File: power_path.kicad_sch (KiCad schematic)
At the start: 0 parts

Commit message: Added TPS631000
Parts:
- added U2: TPS631000DRLR, footprints:SOT50P160X60-8N, symbol symbols:TPS631000DRLR
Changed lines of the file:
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@@
 	(generator_version "10.0")
 	(paper "A4")
+	(symbol
+		(lib_id "symbols:TPS631000DRLR")
+		(at 85.09 72.39 0)
+		(unit 1)
+		(body_style 1)
+		(exclude_from_sim no)
+		(in_bom yes)
+		(on_board yes)
+		(in_pos_files yes)
+		(dnp no)
+		(fields_autoplaced yes)
+		(property "Reference" "U2"
+			(at 85.09 54.61 0)
+			(show_name no)
+			(do_not_autoplace no)
+			(effects
+				(font
+					(size 1.27 1.27)
+				)
+			)
+		)
+		(property "Value" "TPS631000DRLR"
+			(at 85.09 57.15 0)
+			(show_name no)
+			(do_not_autoplace no)
+			(effects
+				(font
+					(size 1.27 1.27)
+				)
+			)
+		)
+		(property "Footprint" "footprints:SOT50P160X60-8N"
+			(at 85.09 72.39 0)
+			(hide yes)
+			(show_name no)
+			(do_not_autoplace no)
+			(effects
+				(font
+					(size 1.27 1.27)
+				)
+				(justify bottom)
+			)
+		)
+		(property "Datasheet" ""
+			(at 85.09 72.39 0)
+			(hide yes)
+			(show_name no)
+			(do_not_autoplace no)
+			(effects
+				(font
+					(size 1.27 1.27)
+				)
+			)
+		)
+		(property "Description" "1.5-A output current, high-power-density buck-boost converter"
+			(at 85.09 72.39 0)
+			(hide yes)
+			(show_name no)
+			(do_not_autoplace no)
+			(effects
+				(font
+					(size 1.27 1.27)
+				)
+				(justify bottom)
+			)
+		)
+		(property "DigiKey_Part_Number" "296-TPS631000DRLRCT-ND"
+			(at 85.09 72.39 0)
+			(hide yes)
+			(show_name no)
+			(do_not_autoplace no)
+			(effects
+				(font
+					(size 1.27 1.27)
+				)
+				(justify bottom)
+			)
+		)
+		(property "SnapEDA_Link" "https://www.snapeda.com/parts/TPS631000DRLR/Texas+Instruments/view-part/?ref=snap"
+			(at 85.09 72.39 0)
+			(hide yes)
+			(show_name no)
+			(do_not_autoplace no)
+			(effects
+				(font
+					(size 1.27 1.27)
+				)
+				(justify bottom)
+			)
+		)
+		(property "SNAPEDA_PACKAGE_ID" "124400"
+			(at 85.09 72.39 0)
+			(hide yes)
+			(show_name no)
+			(do_not_autoplace no)
+			(effects
+				(font
+					(size 1.27 1.27)
+				)
+				(justify bottom)
+			)
+		)
+		(property "Package" "SOT-583 Texas Instruments"
+			(at 85.09 72.39 0)
+			(hide yes)
+			(show_name no)
+			(do_not_autoplace no)
+			(effects
+				(font
+					(size 1.27 1.27)
+				)
+				(justify bottom)
+			)
+		)
+		(property "Check_prices" "https://www.snapeda.com/parts/TPS631000DRLR/Texas+Instruments/view-part/?ref=eda"
+			(at 85.09 72.39 0)
+			(hide yes)
+			(show_name no)
+			(do_not_autoplace no)
+			(effects
+				(font
+					(size 1.27 1.27)
+				)
+				(justify bottom)
+			)
+		)
+		(property "STANDARD" "IPC 7351B"
+			(at 85.09 72.39 0)
+			(hide yes)
+			(show_name no)
+			(do_not_autoplace no)
+			(effects
+				(font
+					(size 1.27 1.27)
+				)
+				(justify bottom)
+			)
+		)
+		(property "PARTREV" "B"
+			(at 85.09 72.39 0)
+			(hide yes)
+			(show_name no)
+			(do_not_autoplace no)
+			(effects
+				(font
+					(size 1.27 1.27)
+				)
+				(justify bottom)
+			)
+		)
+		(property "MF" "Texas Instruments"
+			(at 85.09 72.39 0)
+			(hide yes)
+			(show_name no)
+			(do_not_autoplace no)
+			(effects
+				(font
+					(size 1.27 1.27)
+				)
+				(justify bottom)
+			)
+		)
+		(property "MP" "TPS631000DRLR"
+			(at 85.09 72.39 0)
+			(hide yes)
+			(show_name no)
+			(do_not_autoplace no)
+			(effects
+				(font
+					(size 1.27 1.27)
+				)
+				(justify bottom)
+			)
+		)
+		(property "MANUFACTURER" "Texas Instruments"
+			(at 85.09 72.39 0)
+			(hide yes)
+			(show_name no)
+			(do_not_autoplace no)
+			(effects
+				(font
+					(size 1.27 1.27)
+				)
+				(justify bottom)
+			)
+		)
+		(property "MAXIMUM_PACKAGE_HEIGHT" "0.6mm"
+			(at 85.09 72.39 0)
+			(hide yes)
+			(show_name no)
+			(do_not_autoplace no)
+			(effects
+				(font
+					(size 1.27 1.27)
+				)
+				(justify bottom)
+			)
+		)
+		(property "LCSC" "C5219190"
+			(at 85.09 72.39 0)
+			(hide yes)
+			(show_name no)
+			(do_not_autoplace no)
+			(effects
+				(font
+					(size 1.27 1.27)
+				)
+			)
+		)
+		(pin "7"
+		)
+		(pin "8"
+		)
+		(pin "6"
+		)
+		(pin "4"
+		)
+		(pin "3"
+		)
+		(pin "2"
+		)
+		(pin "5"
+		)
+		(pin "1"
+		)
+		(instances
+			(project "pedal"
+				(path "/e2443317-b83f-4e66-ac79-3186c6d613f3/487ab5a8-1c1d-4a3e-8f62-a21afc38e9a3"
+					(reference "U2")
+					(unit 1)
+				)
+			)
+		)
+	)
 )

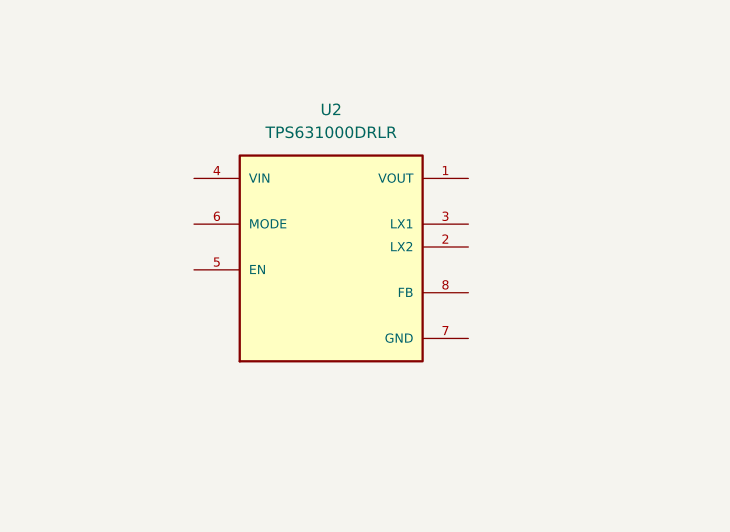
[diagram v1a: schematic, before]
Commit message: buck boost regulator schematic done
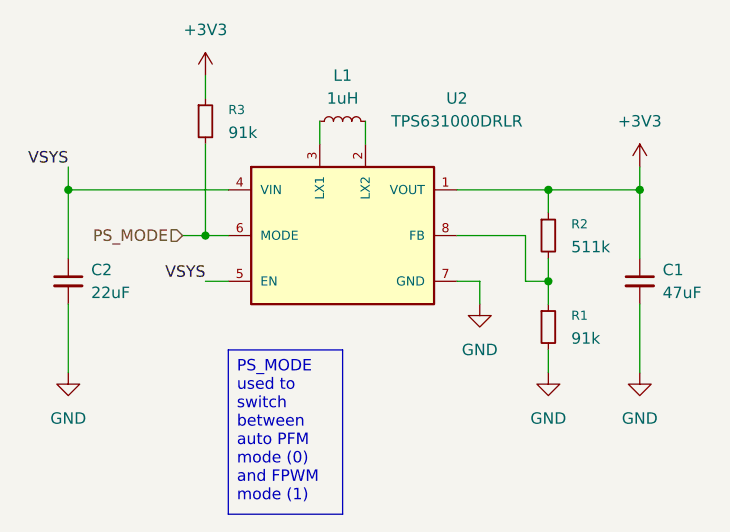
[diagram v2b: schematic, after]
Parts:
- added C1: 47uF, Capacitor_SMD:C_0805_2012Metric, symbol Device:C_Small
- added C2: 22uF, Capacitor_SMD:C_1206_3216Metric, symbol Device:C_Small
- added L1: 1uH, Inductor_SMD:L_1008_2520Metric, symbol Device:L_Small
- added R1, R3: 91k, Resistor_SMD:R_0402_1005Metric, symbol Device:R_Small
- added R2: 511k, Resistor_SMD:R_0402_1005Metric, symbol Device:R_Small
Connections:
- net +3V3: now reaches U2.1 (VOUT)
- net +3V3: now also C1.1, R2.1, R3.1
- net at U2.2 (LX2): now also L1.2
- net at U2.3 (LX1): now also L1.1
- net VSYS: now reaches U2.4 (VIN)
- net VSYS: now also U2.5 (EN), C2.1
- net PS_MODE: now reaches U2.6 (MODE)
- net PS_MODE: now also R3.2
- net GND: now reaches U2.7 (GND)
- net GND: now also C1.2, C2.2, R1.2
- net at U2.8 (FB): now also R1.1, R2.2
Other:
- moved on the sheet: U2

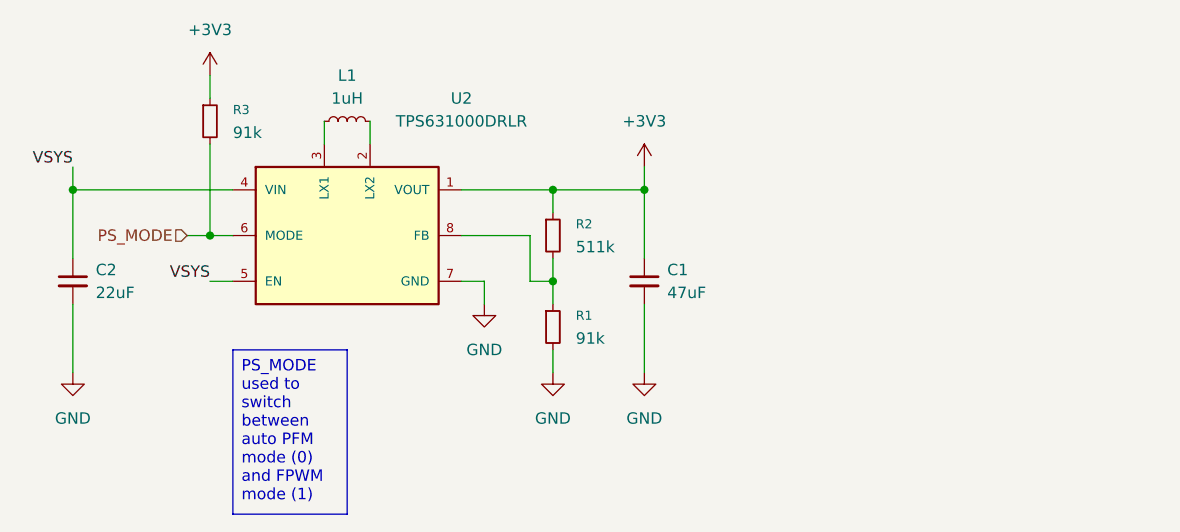
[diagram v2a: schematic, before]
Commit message: added LDO for LCD rail
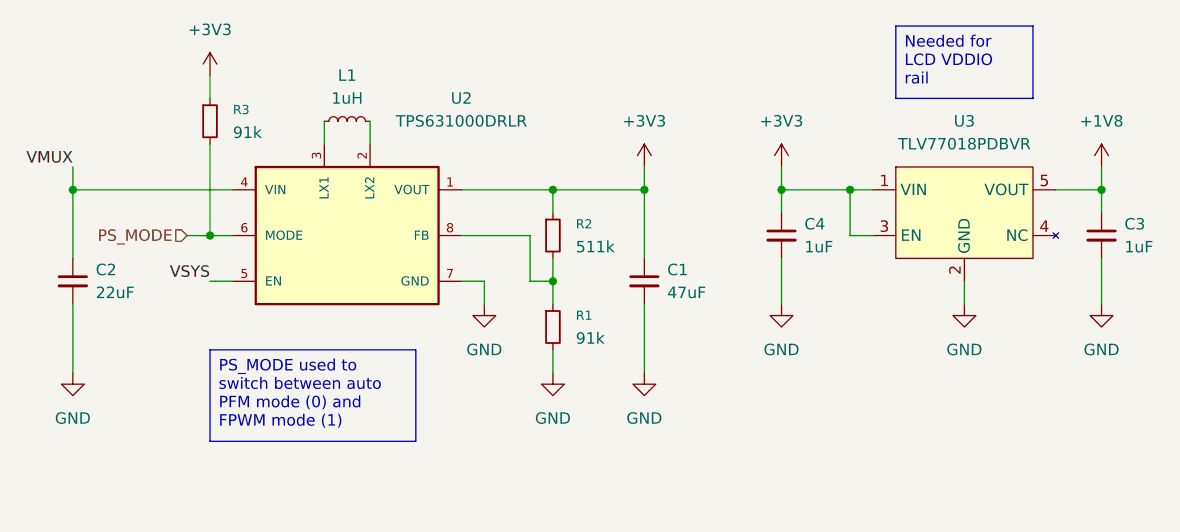
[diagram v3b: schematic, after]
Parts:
- added C3, C4: 1uF, Capacitor_SMD:C_0402_1005Metric, symbol Device:C_Small
- added U3: TLV77018PDBVR, Package_TO_SOT_SMD:SOT-23-5, symbol symbols:TLV77018PDBVR
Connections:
- net +3V3: now also C4.1, U3.1 (VIN), U3.3 (EN)
- net GND: now also C3.2, C4.2, U3.2 (GND)
- net VSYS: no longer C2.1, U2.4 (VIN)
- new net +1V8: C3.1, U3.5 (VOUT)
- new net VMUX: C2.1, U2.4 (VIN)

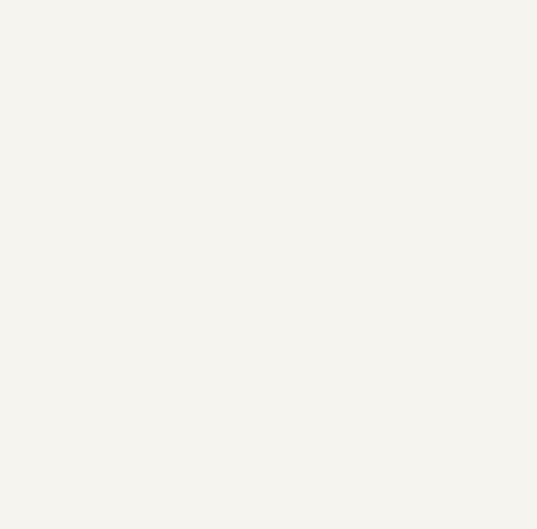
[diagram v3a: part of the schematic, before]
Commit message: add tps2121 power mux component
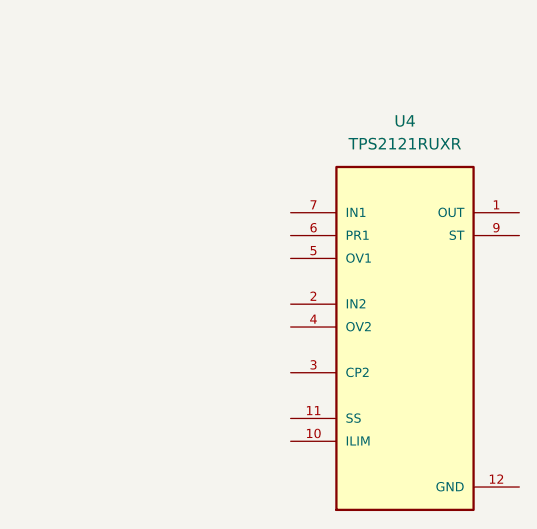
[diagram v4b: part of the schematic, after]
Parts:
- added U4: TPS2121RUXR, footprints:IC_TPS2121RUXR, symbol symbols:TPS2121RUXR
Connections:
- new net: U4.1 (OUT), U4.1_1 (OUT), U4.8 (OUT), U4.8_1 (OUT)
- new net: U4.2 (IN2), U4.2_1 (IN2)
- new net: U4.7 (IN1), U4.7_1 (IN1)
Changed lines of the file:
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@@
+	)
+	(symbol
+		(lib_id "symbols:TPS2121RUXR")
+		(at 223.52 81.28 0)
+		(unit 1)
+		(body_style 1)
+		(exclude_from_sim no)
+		(in_bom yes)
+		(on_board yes)
+		(in_pos_files yes)
+		(dnp no)
+		(fields_autoplaced yes)
+		(property "Reference" "U4"
+			(at 223.52 55.88 0)
+			(show_name no)
+			(do_not_autoplace no)
+			(effects
+				(font
+					(size 1.27 1.27)
+				)
+			)
+		)
+		(property "Value" "TPS2121RUXR"
+			(at 223.52 58.42 0)
+			(show_name no)
+			(do_not_autoplace no)
+			(effects
+				(font
+					(size 1.27 1.27)
+				)
+			)
+		)
+		(property "Footprint" "footprints:IC_TPS2121RUXR"
+			(at 223.52 81.28 0)
+			(hide yes)
+			(show_name no)
+			(do_not_autoplace no)
+			(effects
+				(font
+					(size 1.27 1.27)
+				)
+				(justify bottom)
+			)
+		)
+		(property "Datasheet" ""
+			(at 223.52 81.28 0)
+			(hide yes)
+			(show_name no)
+			(do_not_autoplace no)
+			(effects
+				(font
+					(size 1.27 1.27)
+				)
+			)
+		)
+		(property "Description" "2.7-V to 22-V, 56-mΩ, 4.5-A, power mux with seamless switchover"
+			(at 223.52 81.28 0)
+			(hide yes)
+			(show_name no)
+			(do_not_autoplace no)
+			(effects
+				(font
+					(size 1.27 1.27)
+				)
+				(justify bottom)
+			)
+		)
+		(property "MF" "Texas Instruments"
+			(at 223.52 81.28 0)
+			(hide yes)
+			(show_name no)
+			(do_not_autoplace no)
+			(effects
+				(font
+					(size 1.27 1.27)
+				)
+				(justify bottom)
+			)
+		)
+		(property "Package" "VQFN-HR-12 Texas Instruments"
+			(at 223.52 81.28 0)
+			(hide yes)
+			(show_name no)
+			(do_not_autoplace no)
+			(effects
+				(font
+					(size 1.27 1.27)
+				)
+				(justify bottom)
+			)
+		)
+		(property "Price" "None"
+			(at 223.52 81.28 0)
+			(hide yes)
+			(show_name no)
+			(do_not_autoplace no)
+			(effects
+				(font
+					(size 1.27 1.27)
+				)
+				(justify bottom)
+			)
+		)
+		(property "Check_prices" "https://www.snapeda.com/parts/TPS2121RUXR/Texas+Instruments/view-part/?ref=eda"
+			(at 223.52 81.28 0)
+			(hide yes)
+			(show_name no)
+			(do_not_autoplace no)
+			(effects
+				(font
+					(size 1.27 1.27)
+				)
+				(justify bottom)
+			)
+		)
+		(property "STANDARD" "Manufacturer Recommendations"
+			(at 223.52 81.28 0)
+			(hide yes)
+			(show_name no)
+			(do_not_autoplace no)
+			(effects
+				(font
+					(size 1.27 1.27)
+				)
+				(justify bottom)
+			)
+		)
+		(property "SnapEDA_Link" "https://www.snapeda.com/parts/TPS2121RUXR/Texas+Instruments/view-part/?ref=snap"
+			(at 223.52 81.28 0)
+			(hide yes)
+			(show_name no)
+			(do_not_autoplace no)
+			(effects
+				(font
+					(size 1.27 1.27)
+				)
+				(justify bottom)
+			)
+		)
+		(property "MP" "TPS2121RUXR"
+			(at 223.52 81.28 0)
+			(hide yes)
+			(show_name no)
+			(do_not_autoplace no)
+			(effects
+				(font
+					(size 1.27 1.27)
+				)
+				(justify bottom)
+			)
+		)
+		(property "Availability" "In Stock"
+			(at 223.52 81.28 0)
+			(hide yes)
+			(show_name no)
+			(do_not_autoplace no)
+			(effects
+				(font
+					(size 1.27 1.27)
+				)
+				(justify bottom)
+			)
+		)
+		(property "MANUFACTURER" "TEXAS INSTRUMENTS"
+			(at 223.52 81.28 0)
+			(hide yes)
+			(show_name no)
+			(do_not_autoplace no)
+			(effects
+				(font
+					(size 1.27 1.27)
+				)
+				(justify bottom)
+			)
+		)
+		(property "LCSC" "C485916"
+			(at 223.52 81.28 0)
+			(hide yes)
+			(show_name no)
+			(do_not_autoplace no)
+			(effects
+				(font
+					(size 1.27 1.27)
+				)
+			)
+		)
+		(pin "8"
+		)
+		(pin "11"
+		)
+		(pin "7_1"
+		)
+		(pin "9"
+		)
+		(pin "10"
+		)
+		(pin "12"
+		)
+		(pin "8_1"
+		)
+		(pin "2"
+		)
+		(pin "5"
+		)
+		(pin "2_1"
+		)
+		(pin "3"
+		)
+		(pin "4"
+		)
+		(pin "7"
+		)
+		(pin "6"
+		)
+		(pin "1"
+		)
+		(pin "1_1"
+		)
+		(instances
+			(project "pedal"
+				(path "/e2443317-b83f-4e66-ac79-3186c6d613f3/487ab5a8-1c1d-4a3e-8f62-a21afc38e9a3"
+					(reference "U4")
+					(unit 1)
+				)
+			)
+		)
 	)
 	(symbol

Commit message: wip
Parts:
- added R4: 56k, Resistor_SMD:R_0402_1005Metric, symbol Device:R_Small
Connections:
- net GND: now also U4.3 (CP2), U4.6 (PR1), R4.2
- net VMUX: now also U4.1 (OUT), U4.1_1 (OUT), U4.8 (OUT), U4.8_1 (OUT)
- net at U4.10 (ILIM): now also R4.1
- net VUSB: now reaches U4.7 (IN1), U4.7_1 (IN1)

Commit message: random silly commit
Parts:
- removed R4: 56k, Resistor_SMD:R_0402_1005Metric, symbol Device:R_Small
- removed U4: TPS2121RUXR, footprints:IC_TPS2121RUXR, symbol symbols:TPS2121RUXR
- added U4: TPS2116DRL, Package_TO_SOT_SMD:SOT-583-8, symbol Power_Management:TPS2116DRL
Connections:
- net VSYS is gone; now on net VMUX: U2.5 (EN)
- net GND: now also U4.1 (GND)
- net VMUX: now also U4.2 (VOUT), U4.7 (VOUT)
- net VUSB: now also U4.3 (VIN1), U4.4 (PR1), U4.5 (MODE)
- new net MUX_STATE: U4.8 (ST)
- new net VBATT: U4.6 (VIN2)
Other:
- note added: "Low: Battery, Hi-Z: USB"
- note added: "Low: PFM, Hi-Z: FPWM"

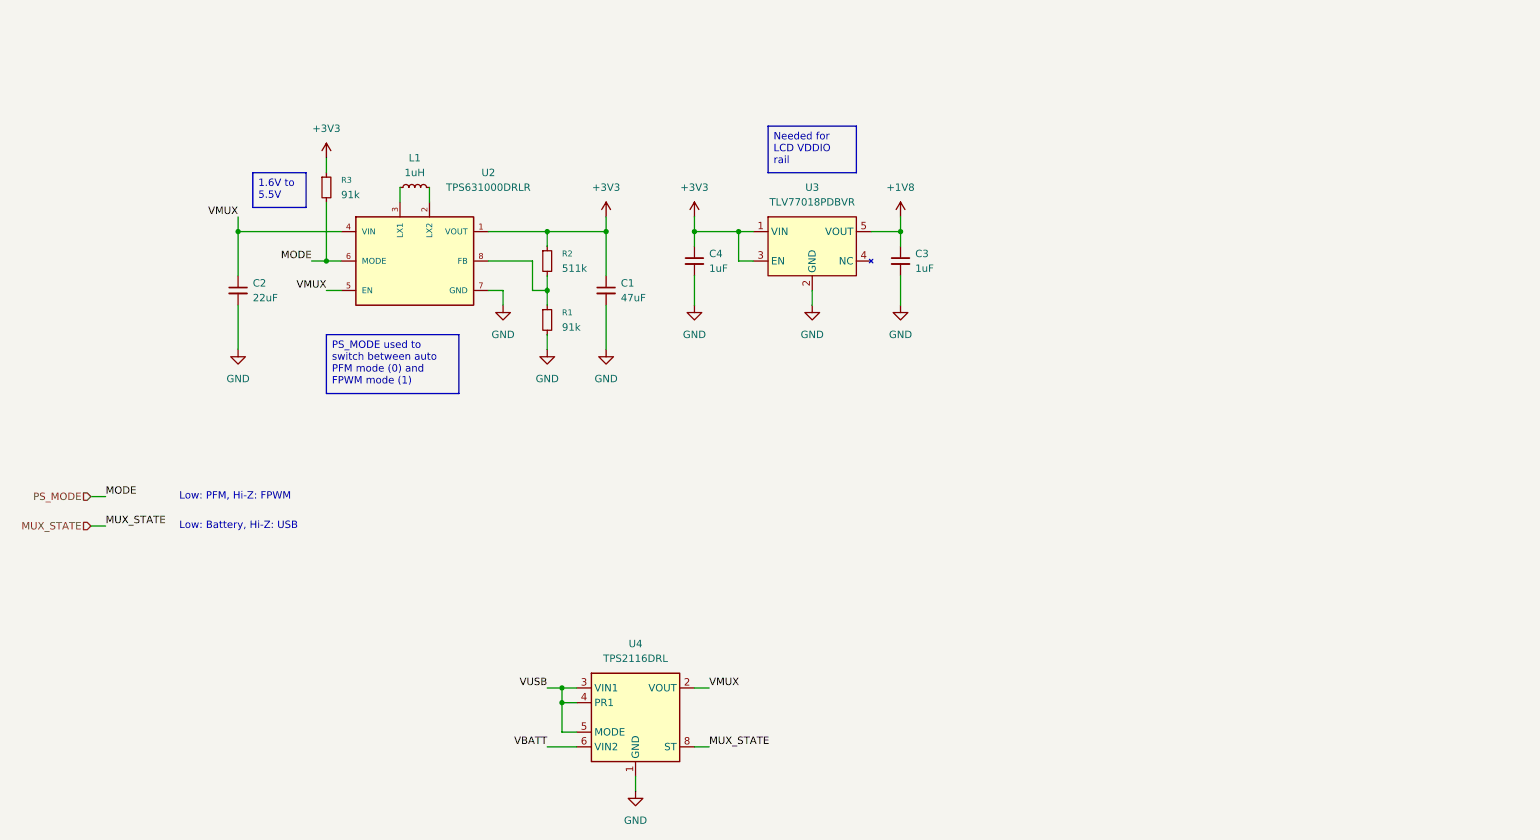
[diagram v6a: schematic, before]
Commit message: add type c receptacle
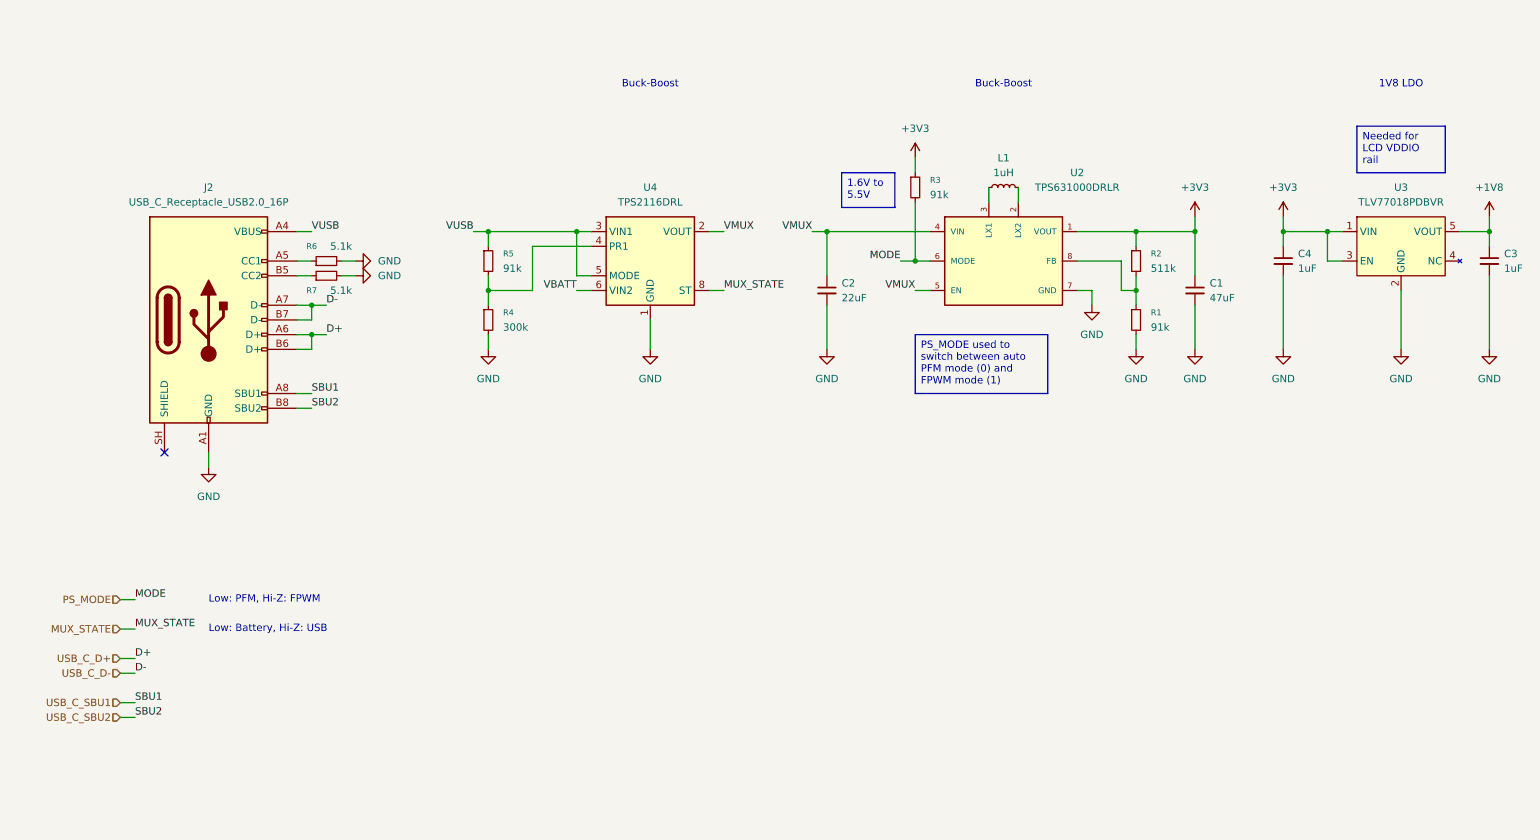
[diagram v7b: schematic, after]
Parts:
- added J2: USB_C_Receptacle_USB2.0_16P, Connector_USB:USB_C_Receptacle_HRO_TYPE-C-31-M-12, symbol Connector:USB_C_Receptacle_USB2.0_16P
- added R4: 300k, Resistor_SMD:R_0402_1005Metric, symbol Device:R_Small
- added R5: 91k, Resistor_SMD:R_0402_1005Metric, symbol Device:R_Small
- added R6, R7: 5.1k, Resistor_SMD:R_0402_1005Metric, symbol Device:R_Small
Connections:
- net GND: now also J2.A1 (GND), J2.A12 (GND), J2.B1 (GND), J2.B12 (GND), R4.2, R6.2, R7.2
- net VUSB: now also J2.A4 (VBUS), J2.A9 (VBUS), J2.B4 (VBUS), J2.B9 (VBUS), R5.1; no longer U4.4 (PR1)
- new net: J2.A5 (CC1), R6.1
- new net: J2.B5 (CC2), R7.1
- new net: R4.1, R5.2, U4.4 (PR1)
- new net USB_C_D+: J2.A6 (D+), J2.B6 (D+)
- new net USB_C_D-: J2.A7 (D-), J2.B7 (D-)
- new net USB_C_SBU1: J2.A8 (SBU1)
- new net USB_C_SBU2: J2.B8 (SBU2)
- no-connect marks 0 -> 1
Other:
- note added: "1V8 LDO"
- note added: "Buck-Boost"
- moved on the sheet: C1, C2, C3, C4, L1, R1, R2, R3, U2, U3, U4

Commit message: add esd protection to usb port
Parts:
- added U5, U6: USBLC6-2SC6, Package_TO_SOT_SMD:SOT-23-6, symbol Power_Protection:USBLC6-2SC6
- J2: LCSC (none) -> C165948
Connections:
- net GND: now also U5.2 (GND), U6.2 (GND)
- net USB_C_D+: now also U5.1 (I/O1), U5.6 (I/O1)
- net USB_C_D-: now also U5.3 (I/O2), U5.4 (I/O2)
- net USB_C_SBU1: now also U6.1 (I/O1), U6.6 (I/O1)
- net USB_C_SBU2: now also U6.3 (I/O2), U6.4 (I/O2)
- net VUSB: now also U5.5 (VBUS), U6.5 (VBUS)
